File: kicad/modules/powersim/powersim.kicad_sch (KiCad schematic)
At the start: 8 parts, among them J1 Bus_PCI_Express_x1, J6 USB_C_Receptacle_USB2.0_16P, U1 AP63203WU

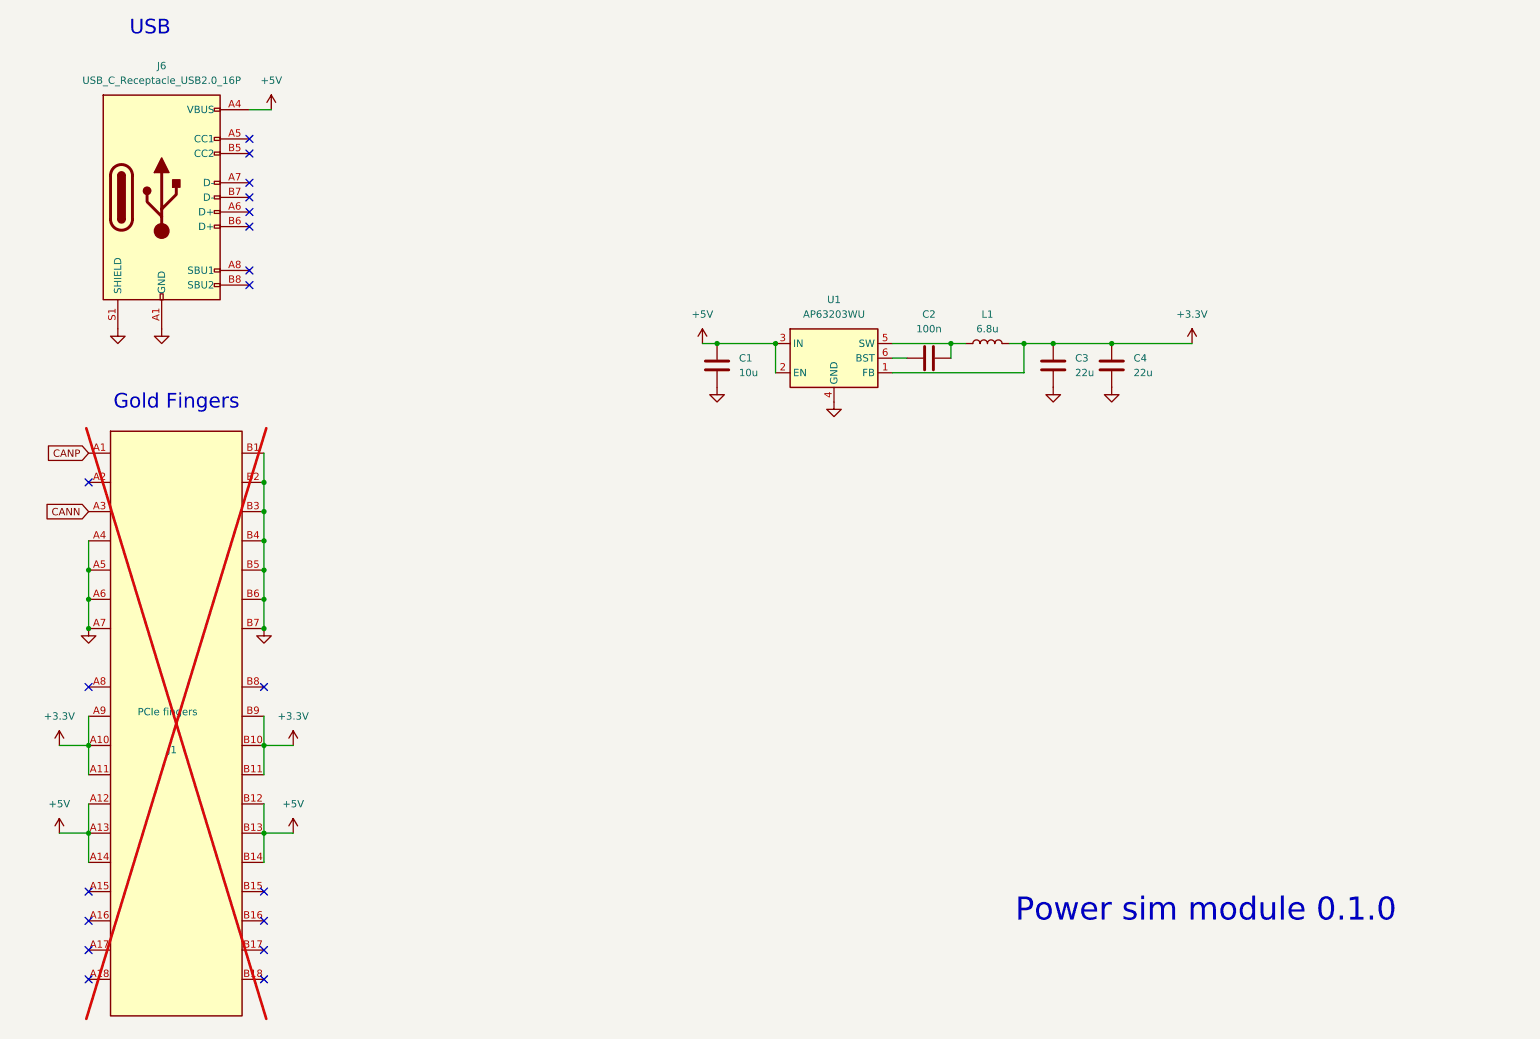
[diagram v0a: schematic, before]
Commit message: powersim: finish PCB
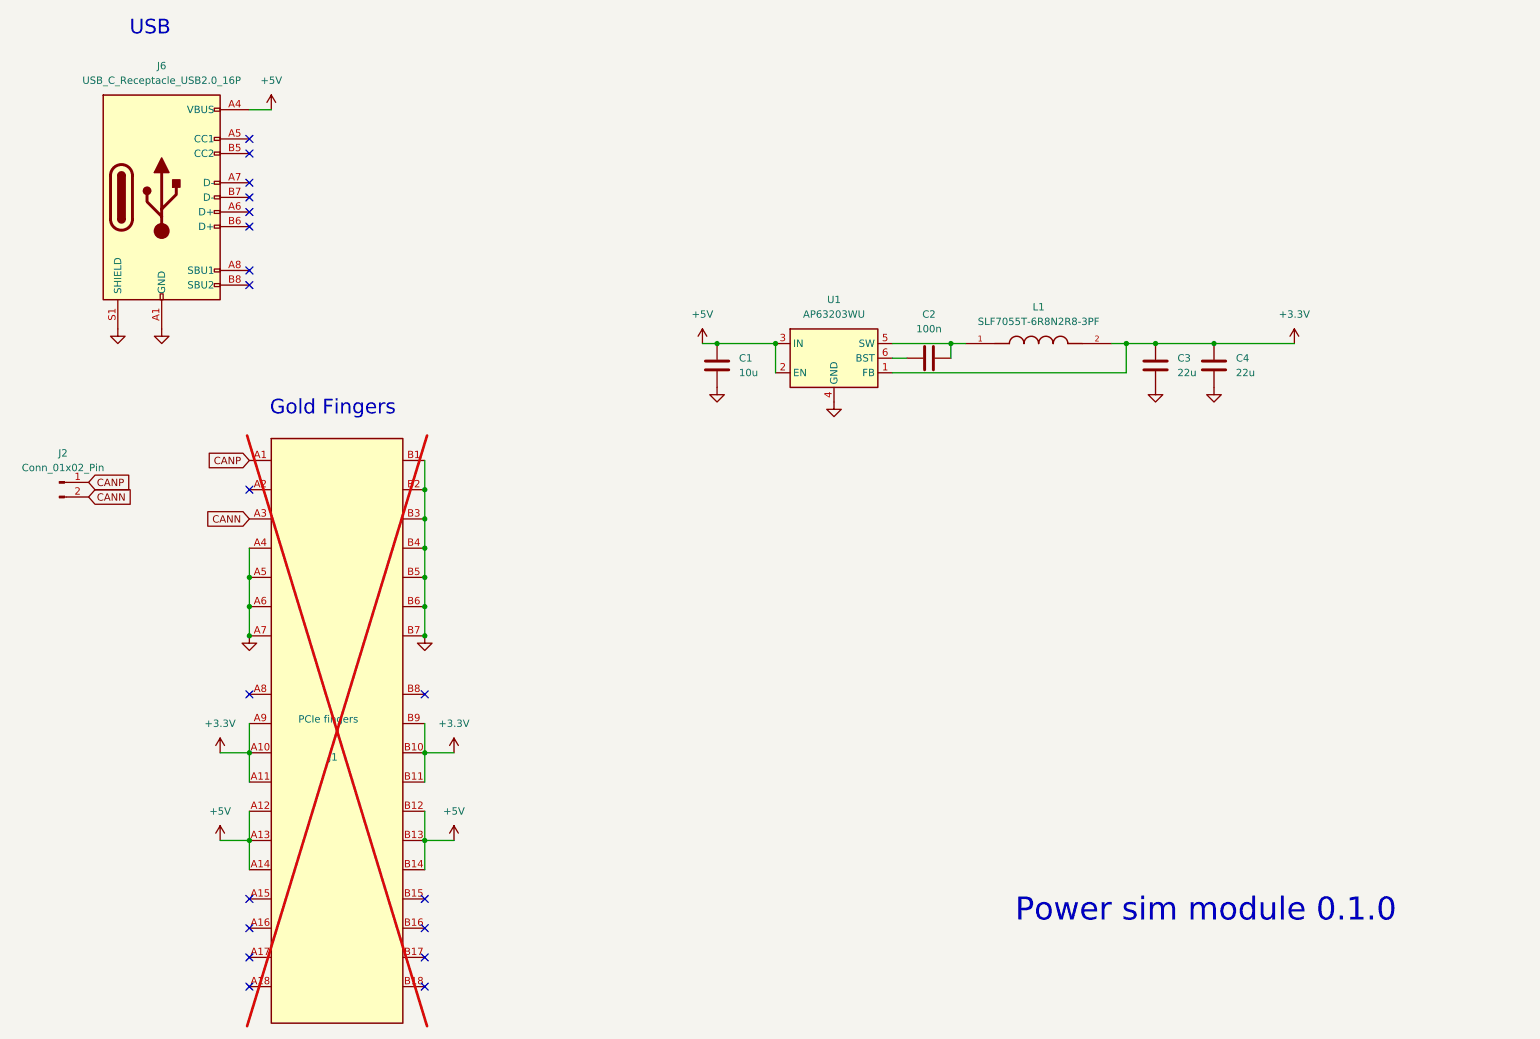
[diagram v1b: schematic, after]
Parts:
- removed L1: 6.8u, symbol Device:L
- added J2: Conn_01x02_Pin, Connector_PinHeader_2.54mm:PinHeader_1x02_P2.54mm_Vertical, symbol Connector:Conn_01x02_Pin
- added L1: SLF7055T-6R8N2R8-3PF, SLF7055T-6R8N2R8-3PF:IND_SLF7055T-6R8N2R8-3PF, symbol SLF7055T-6R8N2R8-3PF:SLF7055T-6R8N2R8-3PF
- C1: footprint (none) -> Capacitor_SMD:C_0402_1005Metric; JLC Link (none) -> https://jlcpcb.com/partdetail/16204-CL05A106MQ5NUNC/C15525; LCSC Part # (none) -> C15525; basic? (none) -> yes; info (none) -> 10uF; price (none) -> C$0.0056
- C2: footprint (none) -> Capacitor_SMD:C_0402_1005Metric; JLC Link (none) -> https://jlcpcb.com/partdetail/291005-CL05B104KB54PNC/C307331; LCSC Part # (none) -> C307331; basic? (none) -> yes; info (none) -> 100nF
- C3, C4: footprint (none) -> Capacitor_SMD:C_0603_1608Metric; JLC Link (none) -> https://jlcpcb.com/partdetail/60514-CL10A226MQ8NRNC/C59461; LCSC Part # (none) -> C59461; basic? (none) -> yes; info (none) -> 22uF; price (none) -> C$0.0102
- U1: info (none) -> Buck Converter
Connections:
- net +3.3V: now also L1.2
- net CANN: now also J2.2 (Pin_2)
- net CANP: now also J2.1 (Pin_1)
- net at C2.2, U1.5 (SW): now also L1.1
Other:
- moved on the sheet: C3, C4, J1
